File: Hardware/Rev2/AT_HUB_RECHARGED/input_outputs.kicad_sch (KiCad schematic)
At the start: 25 parts, among them J10 IN3, J11 IN4, J12 IN5, J3 OUT1, J4 OUT2, J5 OUT3, J6 OUT4, J7 OUT5, J8 IN1, J9 IN2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

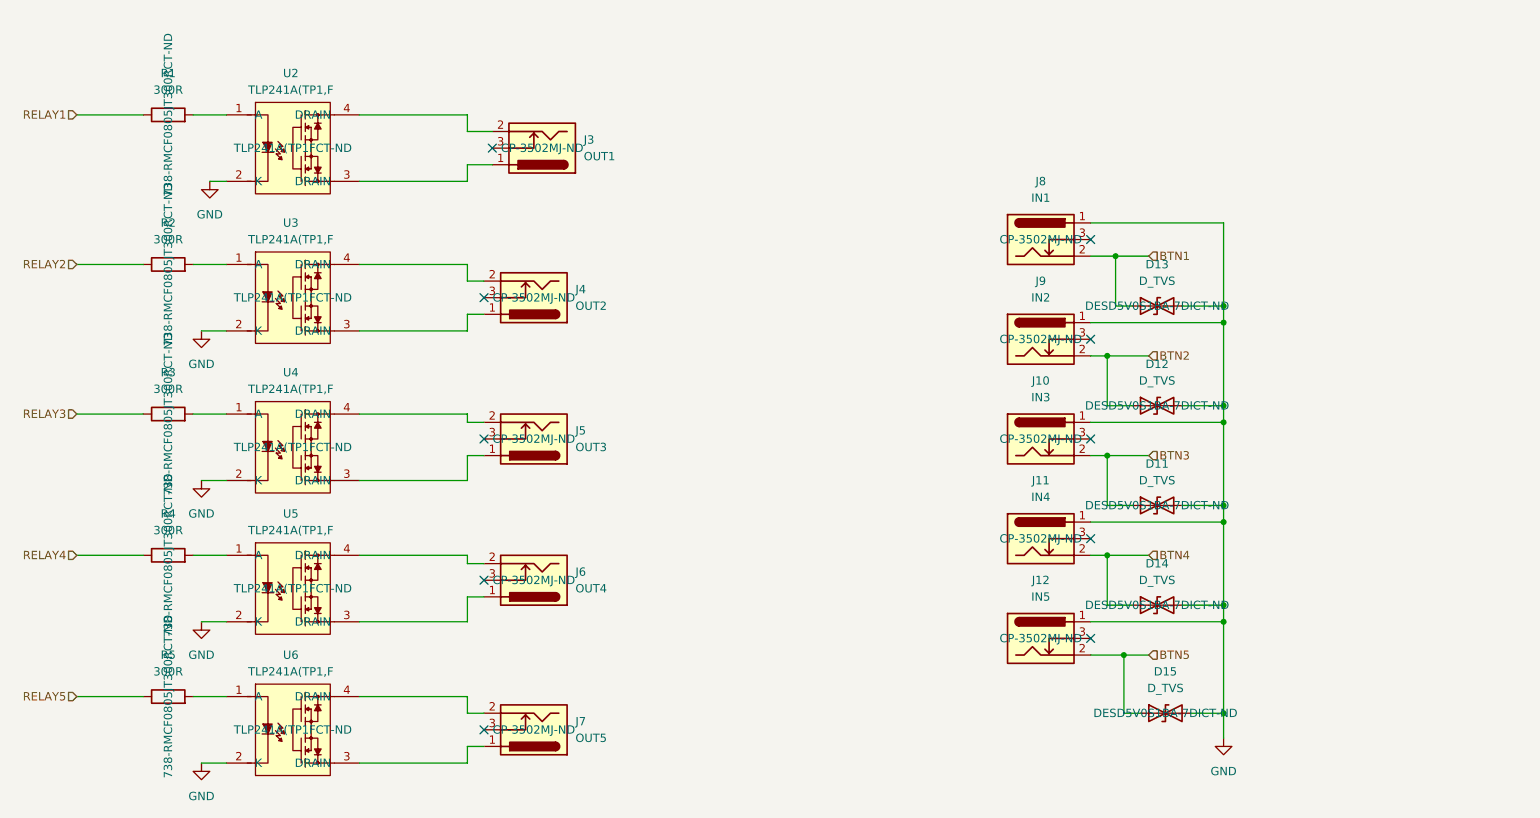
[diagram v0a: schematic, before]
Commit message: Added new protections and load sharing for lipo, also changed inductor to be autoplaced
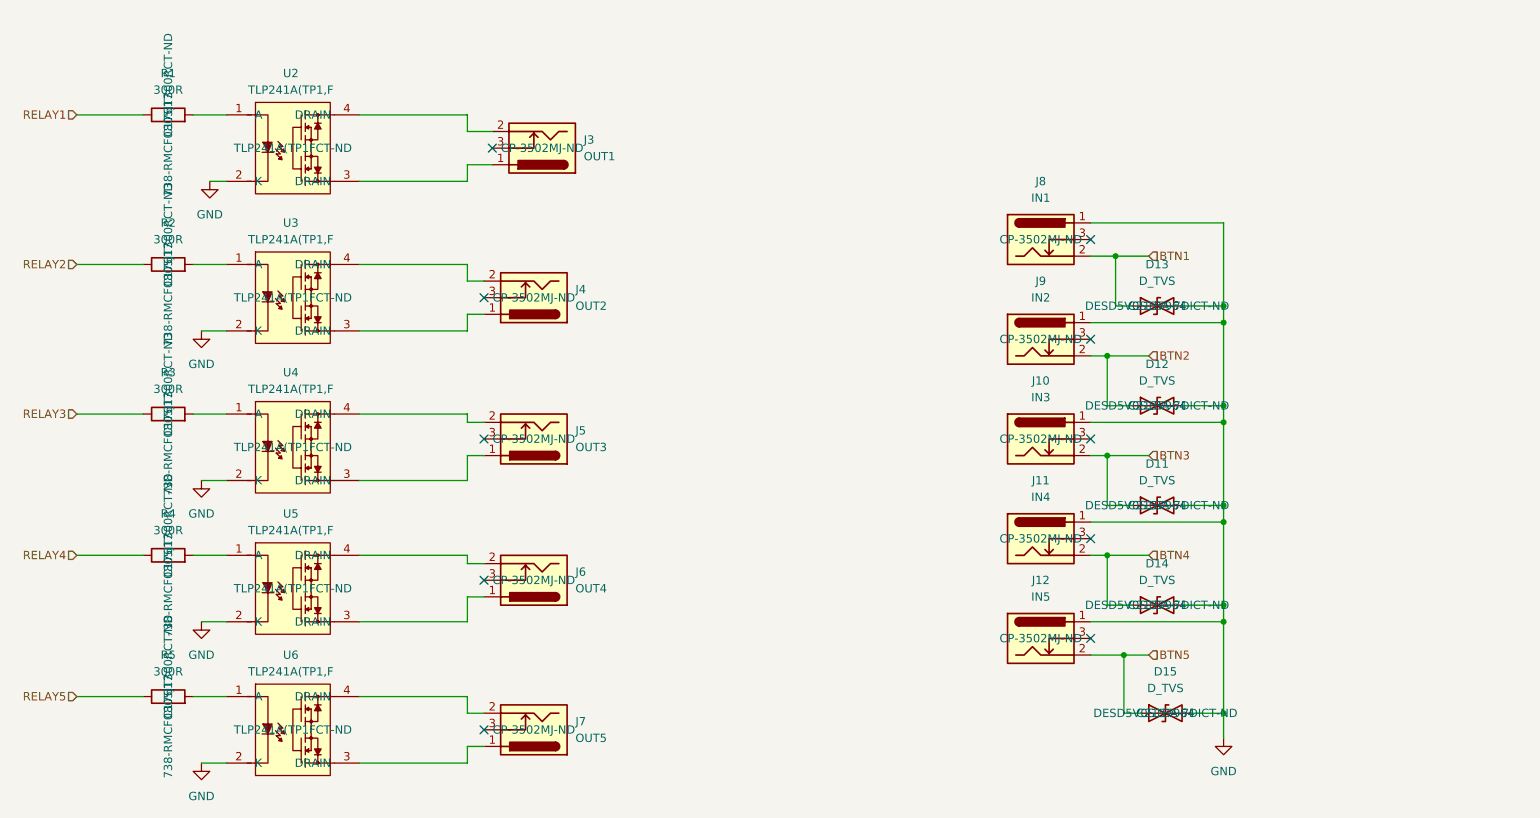
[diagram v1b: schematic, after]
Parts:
- D11, D12, D13, D14, D15: LCSC (none) -> C2157964
- R1, R2, R3, R4, R5: LCSC (none) -> C17617

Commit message: Done the design will verify
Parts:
- added R31, R32, R33, R34, R35: 10k, Resistor_SMD:R_0402_1005Metric, symbol Device:R
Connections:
- net BTN1: now also R31.2
- net BTN2: now also R34.2
- net BTN3: now also R35.2
- net BTN4: now also R33.2
- net BTN5: now also R32.2
- new net +3V3: R31.1, R32.1, R33.1, R34.1, R35.1
